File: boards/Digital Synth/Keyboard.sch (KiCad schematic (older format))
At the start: 50 parts, among them SW1 C3, SW10 A4, SW11 A#4, SW12 B4, SW13 C4, SW14 C#4, SW15 D4, SW16 D#4, SW17 E4, SW18 F4, SW19 F#4, SW2 C#3, SW20 G4, SW21 G#4, SW22 A5, SW23 A#4, SW24 B5, SW25 C5, SW3 D3, SW4 D#3, SW5 E3, SW6 F3, SW7 F#3, SW8 G3, SW9 G#3

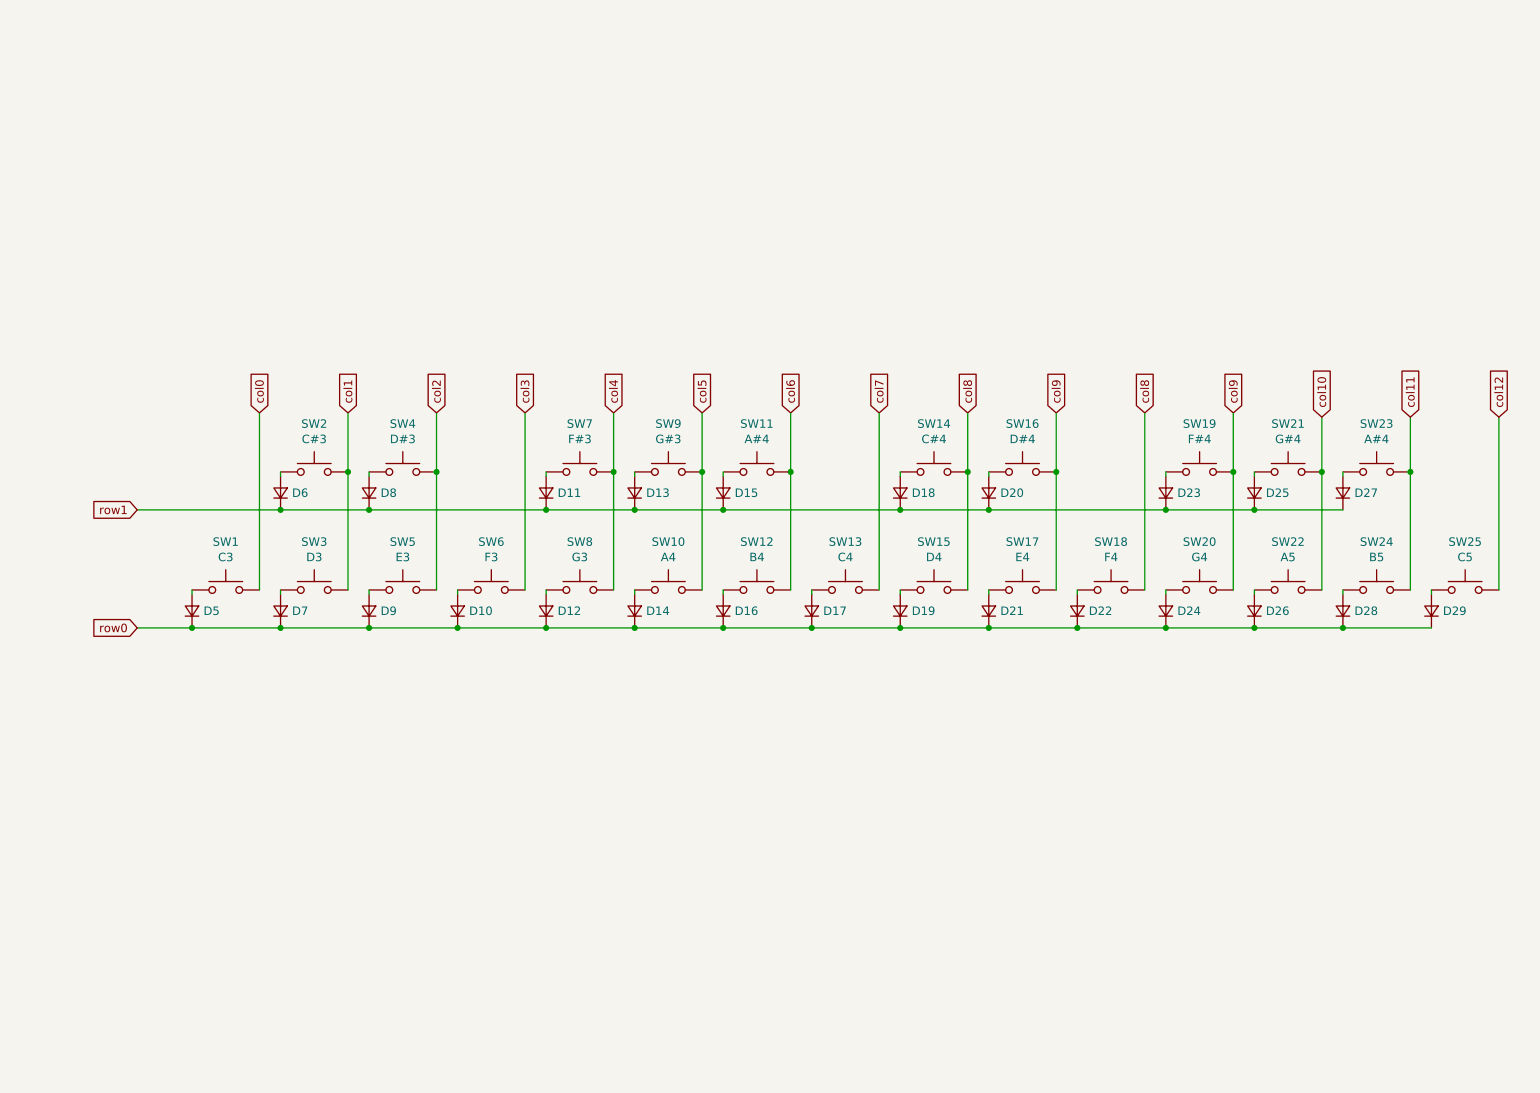
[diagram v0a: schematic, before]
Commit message: progress on layout for DAC and MIDI
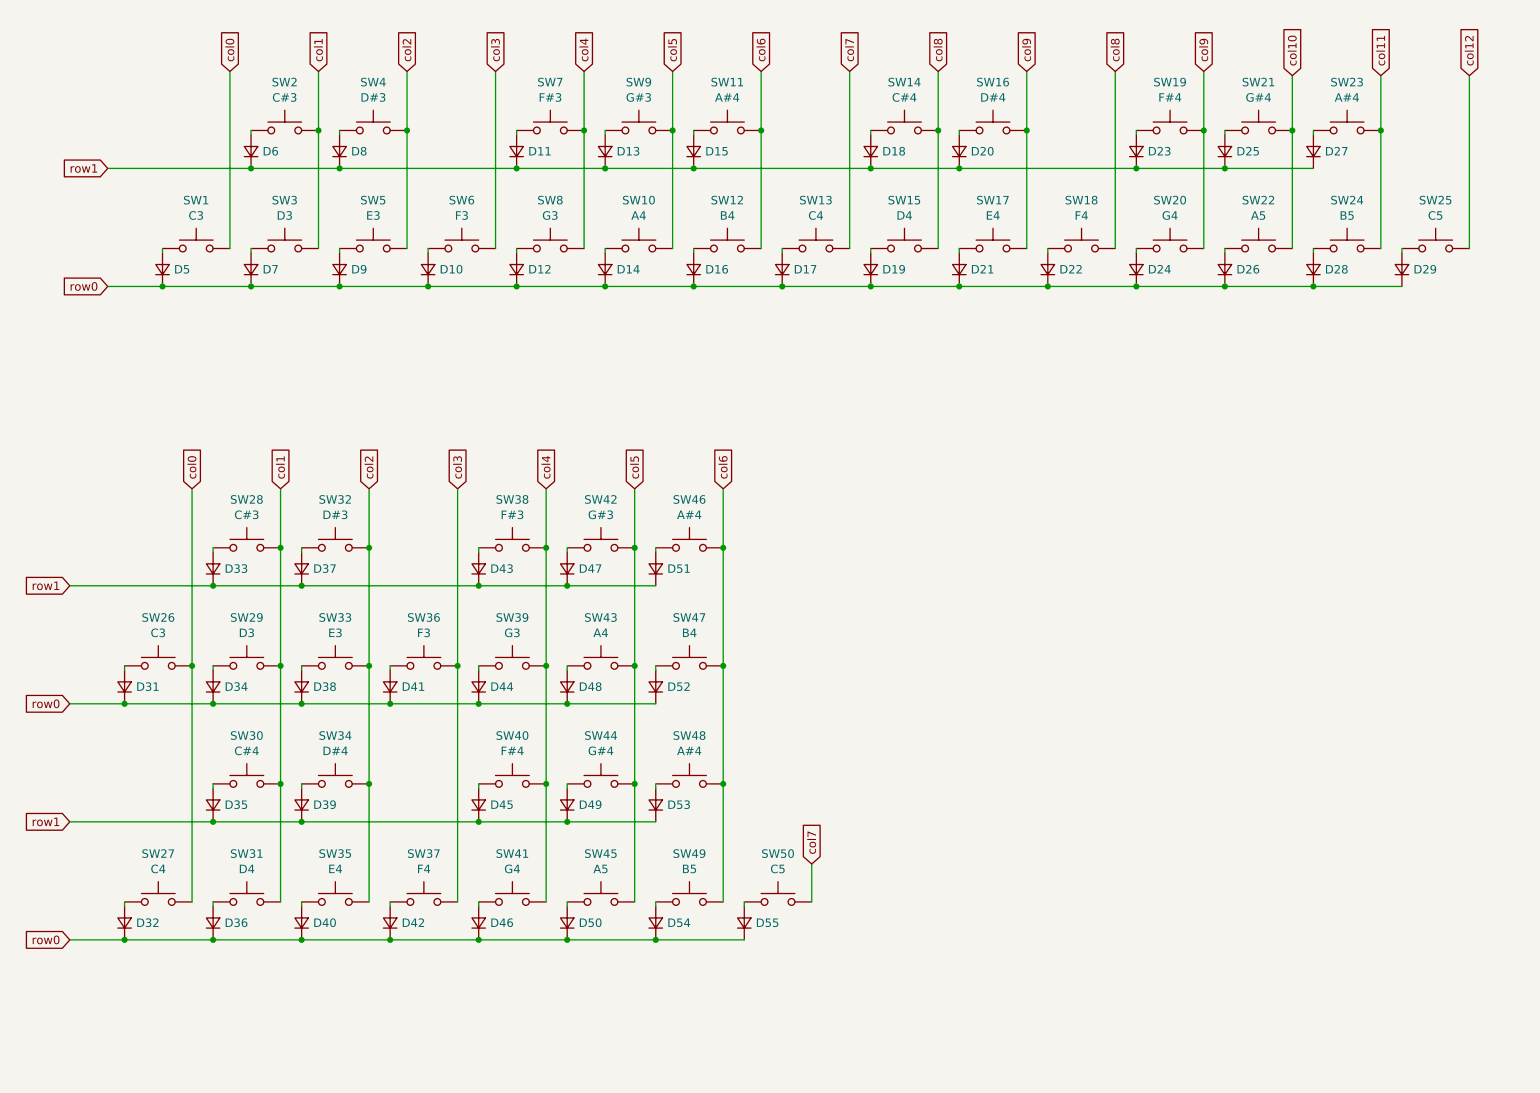
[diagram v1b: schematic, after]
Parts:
- added D31, D32, D33, D34, D35, D36, D37, D38, D39, D40, D41, D42, D43, D44, D45, D46, D47, D48, D49, D50, D51, D52, D53, D54, D55: D_Small, Diode_SMD:D_0805_2012Metric_Pad1.15x1.40mm_HandSolder, symbol device:D_Small
- added SW26: C3, symbol Switch:SW_Push
- added SW27: C4, symbol Switch:SW_Push
- added SW28: C#3, symbol Switch:SW_Push
- added SW29: D3, symbol Switch:SW_Push
- added SW30: C#4, symbol Switch:SW_Push
- added SW31: D4, symbol Switch:SW_Push
- added SW32: D#3, symbol Switch:SW_Push
- added SW33: E3, symbol Switch:SW_Push
- added SW34: D#4, symbol Switch:SW_Push
- added SW35: E4, symbol Switch:SW_Push
- added SW36: F3, symbol Switch:SW_Push
- added SW37: F4, symbol Switch:SW_Push
- added SW38: F#3, symbol Switch:SW_Push
- added SW39: G3, symbol Switch:SW_Push
- added SW40: F#4, symbol Switch:SW_Push
- added SW41: G4, symbol Switch:SW_Push
- added SW42: G#3, symbol Switch:SW_Push
- added SW43: A4, symbol Switch:SW_Push
- added SW44: G#4, symbol Switch:SW_Push
- added SW45: A5, symbol Switch:SW_Push
- added SW46, SW48: A#4, symbol Switch:SW_Push
- added SW47: B4, symbol Switch:SW_Push
- added SW49: B5, symbol Switch:SW_Push
- added SW50: C5, symbol Switch:SW_Push
- D10, D11, D12, D13, D14, D15, D16, D17, D18, D19, D20, D21, D22, D23, D24, D25, D26, D27, D28, D29, D5, D6, D7, D8, D9: footprint (none) -> Diode_SMD:D_0805_2012Metric_Pad1.15x1.40mm_HandSolder
- SW1, SW10, SW11, SW12, SW13, SW14, SW15, SW16, SW17, SW18, SW19, SW2, SW20, SW21, SW22, SW23, SW24, SW25, SW3, SW4, SW5, SW6, SW7, SW8, SW9: footprint (none) -> Keyswitches:Kailh_socket_MX
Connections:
- net col0: now also SW26.2, SW27.2
- net col1: now also SW28.2, SW29.2, SW30.2, SW31.2
- net col2: now also SW32.2, SW33.2, SW34.2, SW35.2
- net col3: now also SW36.2, SW37.2
- net col4: now also SW38.2, SW39.2, SW40.2, SW41.2
- net col5: now also SW42.2, SW43.2, SW44.2, SW45.2
- net col6: now also SW46.2, SW47.2, SW48.2, SW49.2
- net col7: now also SW50.2
- net row0: now also D31.1 (K), D32.1 (K), D34.1 (K), D36.1 (K), D38.1 (K), D40.1 (K), D41.1 (K), D42.1 (K), D44.1 (K), D46.1 (K), D48.1 (K), D50.1 (K), D52.1 (K), D54.1 (K), D55.1 (K)
- net row1: now also D33.1 (K), D35.1 (K), D37.1 (K), D39.1 (K), D43.1 (K), D45.1 (K), D47.1 (K), D49.1 (K), D51.1 (K), D53.1 (K)
- new net: D31.2 (A), SW26.1
- new net: D34.2 (A), SW29.1
- new net: D38.2 (A), SW33.1
- new net: D41.2 (A), SW36.1
- new net: D44.2 (A), SW39.1
- new net: D48.2 (A), SW43.1
- new net: D52.2 (A), SW47.1
- new net: D32.2 (A), SW27.1
- new net: D36.2 (A), SW31.1
- new net: D40.2 (A), SW35.1
- new net: D42.2 (A), SW37.1
- new net: D46.2 (A), SW41.1
- new net: D50.2 (A), SW45.1
- new net: D54.2 (A), SW49.1
- new net: D55.2 (A), SW50.1
- new net: D33.2 (A), SW28.1
- new net: D37.2 (A), SW32.1
- new net: D43.2 (A), SW38.1
- new net: D47.2 (A), SW42.1
- new net: D51.2 (A), SW46.1
- new net: D35.2 (A), SW30.1
- new net: D39.2 (A), SW34.1
- new net: D45.2 (A), SW40.1
- new net: D49.2 (A), SW44.1
- new net: D53.2 (A), SW48.1
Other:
- moved on the sheet: D10, D11, D12, D13, D14, D15, D16, D17, D18, D19, D20, D21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

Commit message: laid out keyboard
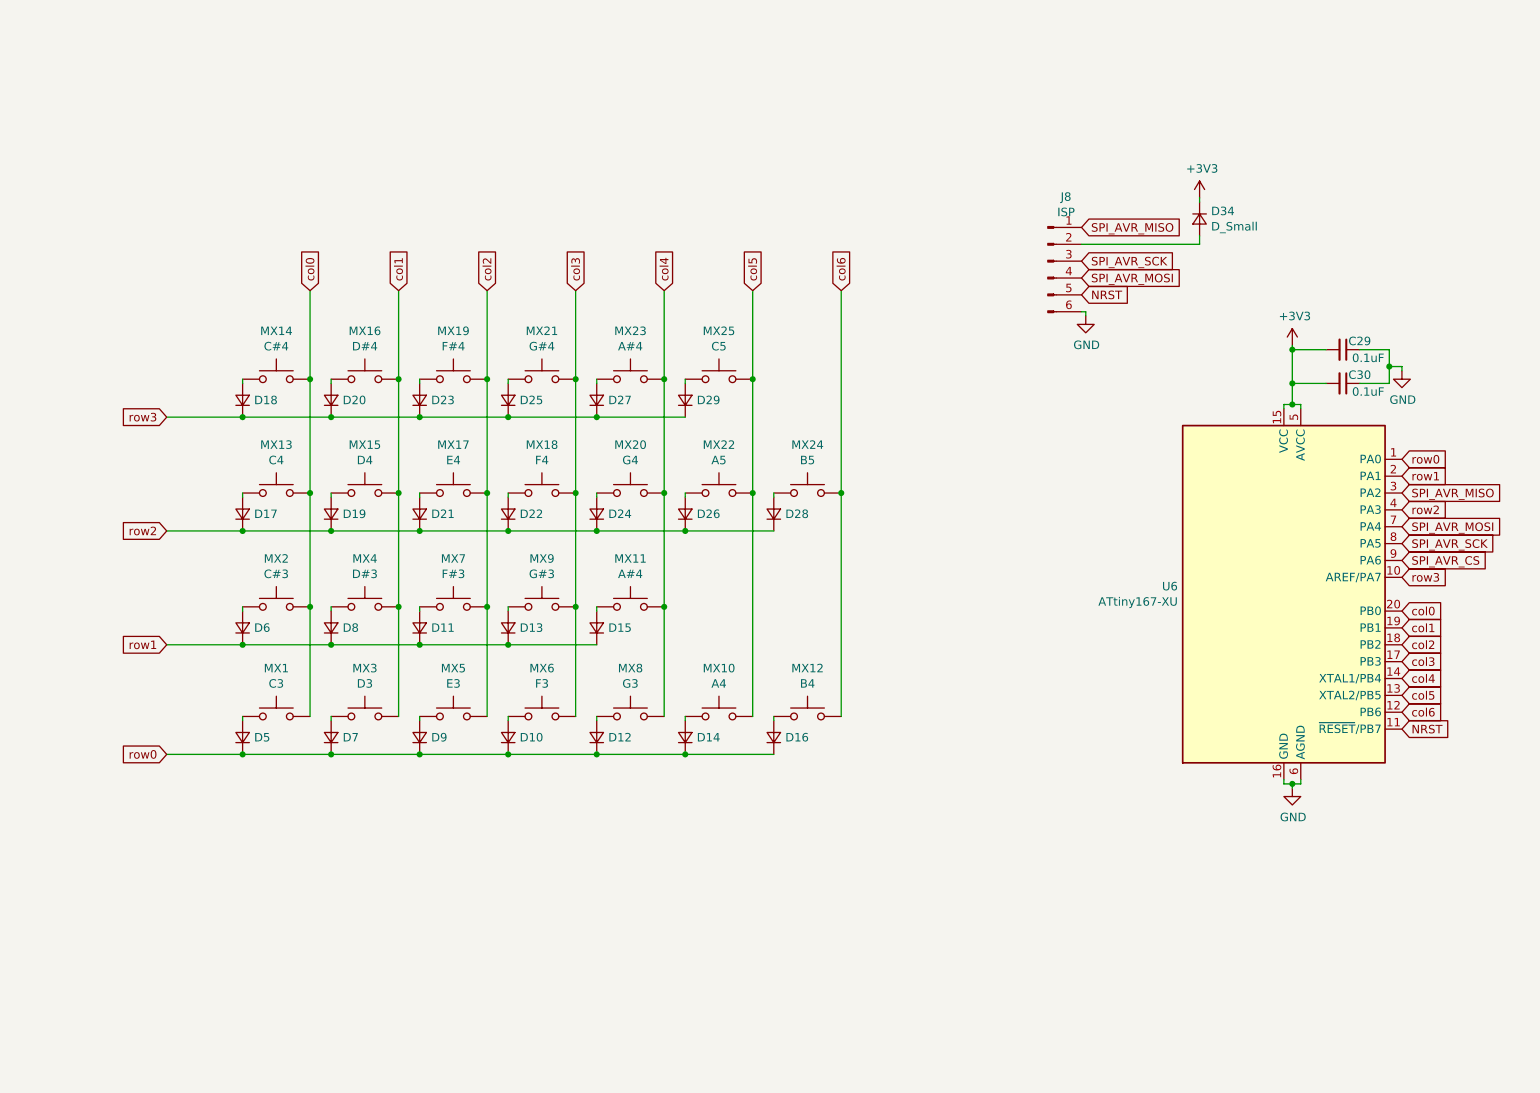
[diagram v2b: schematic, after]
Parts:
- removed D31, D32, D33, D35, D36, D37, D38, D39, D40, D41, D42, D43, D44, D45, D46, D47, D48, D49, D50, D51, D52, D53, D54, D55: D_Small, Diode_SMD:D_0805_2012Metric_Pad1.15x1.40mm_HandSolder, symbol device:D_Small
- removed SW26: C3, symbol Switch:SW_Push
- removed SW27: C4, symbol Switch:SW_Push
- removed SW28: C#3, symbol Switch:SW_Push
- removed SW29: D3, symbol Switch:SW_Push
- removed SW30: C#4, symbol Switch:SW_Push
- removed SW31: D4, symbol Switch:SW_Push
- removed SW32: D#3, symbol Switch:SW_Push
- removed SW33: E3, symbol Switch:SW_Push
- removed SW34: D#4, symbol Switch:SW_Push
- removed SW35: E4, symbol Switch:SW_Push
- removed SW36: F3, symbol Switch:SW_Push
- removed SW37: F4, symbol Switch:SW_Push
- removed SW38: F#3, symbol Switch:SW_Push
- removed SW39: G3, symbol Switch:SW_Push
- removed SW40: F#4, symbol Switch:SW_Push
- removed SW41: G4, symbol Switch:SW_Push
- removed SW42: G#3, symbol Switch:SW_Push
- removed SW43: A4, symbol Switch:SW_Push
- removed SW44: G#4, symbol Switch:SW_Push
- removed SW45: A5, symbol Switch:SW_Push
- removed SW46, SW48: A#4, symbol Switch:SW_Push
- removed SW47: B4, symbol Switch:SW_Push
- removed SW49: B5, symbol Switch:SW_Push
- removed SW50: C5, symbol Switch:SW_Push
- added C29, C30: 0.1uF, Capacitor_SMD:C_0603_1608Metric_Pad1.05x0.95mm_HandSolder, symbol device:C_Small
- added J8: ISP, Connector_PinSocket_2.54mm:PinSocket_2x03_P2.54mm_Horizontal, symbol Connector:Conn_01x06_Male
- added U6: ATtiny167-XU, Package_SO:TSSOP-20_4.4x6.5mm_P0.65mm, symbol MCU_Microchip_ATtiny:ATtiny167-XU
- D34: footprint Diode_SMD:D_0805_2012Metric_Pad1.15x1.40mm_HandSolder -> (none)
- renumbered SW1 to MX1, SW10 to MX10, SW11 to MX11, SW12 to MX12, SW13 to MX13, SW14 to MX14, SW15 to MX15, SW16 to MX16, SW17 to MX17, SW18 to MX18, SW19 to MX19, SW2 to MX2, SW20 to MX20, SW21 to MX21, SW22 to MX22, SW23 to MX23, SW24 to MX24, SW25 to MX25, SW3 to MX3, SW4 to MX4, SW5 to MX5, SW6 to MX6, SW7 to MX7, SW8 to MX8, SW9 to MX9
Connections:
- net col12 is gone; now on net col5: MX25.2
- net col7 is gone; now on net col0: MX13.2
- net col0: now also MX14.2, MX2.2, U6.20 (PB0)
- net col1: now also MX15.2, MX16.2, MX4.2, U6.19 (PB1); no longer MX2.2
- net col2: now also MX17.2, MX19.2, MX7.2, U6.18 (PB2); no longer MX4.2
- net col3: now also MX18.2, MX21.2, MX9.2, U6.17 (PB3)
- net col4: now also MX11.2, MX20.2, MX23.2, U6.14 (XTAL1/PB4); no longer MX7.2
- net col5: now also MX22.2, U6.13 (XTAL2/PB5); no longer MX9.2
- net col6: now also MX24.2, U6.12 (PB6); no longer MX11.2
- net row0: now also U6.1 (PA0); no longer D17.1 (K), D19.1 (K), D21.1 (K), D22.1 (K), D24.1 (K), D26.1 (K), D28.1 (K), D29.1 (K), D34.1 (K)
- net row1: now also U6.2 (PA1); no longer D18.1 (K), D20.1 (K), D23.1 (K), D25.1 (K), D27.1 (K)
- net at D34.2 (A): now also J8.2 (Pin_2)
- removed net col10: MX21.2, MX22.2
- removed net col11: MX23.2, MX24.2
- removed net col8: MX14.2, MX15.2, MX18.2
- removed net col9: MX16.2, MX17.2, MX19.2, MX20.2
- new net +3V3: C29.2, C30.2, D34.1 (K), U6.15 (VCC), U6.5 (AVCC)
- new net GND: C29.1, C30.1, J8.6 (Pin_6), U6.16 (GND), U6.6 (AGND)
- new net NRST: J8.5 (Pin_5), U6.11 (~RESET~/PB7)
- new net SPI_AVR_CS: U6.9 (PA6)
- new net SPI_AVR_MISO: J8.1 (Pin_1), U6.3 (PA2)
- new net SPI_AVR_MOSI: J8.4 (Pin_4), U6.7 (PA4)
- new net SPI_AVR_SCK: J8.3 (Pin_3), U6.8 (PA5)
- new net row2: D17.1 (K), D19.1 (K), D21.1 (K), D22.1 (K), D24.1 (K), D26.1 (K), D28.1 (K), U6.4 (PA3)
- new net row3: D18.1 (K), D20.1 (K), D23.1 (K), D25.1 (K), D27.1 (K), D29.1 (K), U6.10 (AREF/PA7)
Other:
- moved on the sheet: D10, D11, D12, D13, D14, D15, D16, D17, D18, D19, D20, D21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

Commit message: finished routing to avr
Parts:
- J8: footprint Connector_PinSocket_2.54mm:PinSocket_2x03_P2.54mm_Horizontal -> Connector_PinSocket_2.54mm:PinSocket_2x03_P2.54mm_Vertical
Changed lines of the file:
@@
 F 0 "J8" H 7483 2706 50  0000 C CNN
 F 1 "ISP" H 7483 2615 50  0000 C CNN
-F 2 "Connector_PinSocket_2.54mm:PinSocket_2x03_P2.54mm_Horizontal" H 7375 2325 50  0001 C CNN
+F 2 "Connector_PinSocket_2.54mm:PinSocket_2x03_P2.54mm_Vertical" H 7375 2325 50  0001 C CNN
 F 3 "~" H 7375 2325 50  0001 C CNN
 	1    7375 2325

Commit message: almost done with layout
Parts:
- removed D34: D_Small, symbol device:D_Small
- added MXB1, MXB2, MXB3, MXB4, MXB5, MXB6, MXB7, MXB8, MXB9: SW_Push, Keyswitches:Kailh_socket_MX, symbol Switch:SW_Push
- added RV1, RV2, RV3, RV4, RV5, RV6, RV7, RV8: 10k, Potentiometer_THT:Hiletgo, symbol device:R_POT
- D10, D11, D12, D13, D14, D15, D16, D17, D18, D19, D20, D21, D22, D23, D24, D25, D26, D27, D28, D29, D5, D6, D7, D8, D9: footprint Diode_SMD:D_0805_2012Metric_Pad1.15x1.40mm_HandSolder -> Diode_SMD:D_SOD-323
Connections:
- net +3V3: now also J8.2 (Pin_2), RV1.1, RV2.1, RV3.1, RV4.1, RV5.1, RV6.1, RV7.1, RV8.1
- net GND: now also MXB1.2, MXB2.2, MXB3.2, MXB4.2, MXB5.2, MXB6.2, MXB7.2, MXB8.2, MXB9.2, RV1.3, RV2.3, RV3.3, RV4.3, RV5.3, RV6.3, RV7.3, RV8.3
- net SPI_AVR_CS renamed SPI2_CS
- net SPI_AVR_MISO renamed SPI2_MISO
- net SPI_AVR_MOSI renamed SPI2_MOSI
- net SPI_AVR_SCK renamed SPI2_SCK
- new net B1: MXB1.1
- new net B2: MXB2.1
- new net B3: MXB3.1
- new net B4: MXB4.1
- new net B5: MXB5.1
- new net B6: MXB6.1
- new net B7: MXB7.1
- new net B8: MXB8.1
- new net B9: MXB9.1
- new net RV1: RV1.2
- new net RV2: RV2.2
- new net RV3: RV3.2
- new net RV4: RV4.2
- new net RV5: RV5.2
- new net RV6: RV6.2
- new net RV7: RV7.2
- new net RV8: RV8.2
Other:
- note added: "2-octave Keyboard"
- note added: "Buttons"
- note added: "Pots"
- moved on the sheet: D10, D11, D12, D13, D14, D15, D16, D17, D18, D19, D20, D21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
